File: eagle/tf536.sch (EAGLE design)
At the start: 74 parts, among them IC1 MC68030, IC10 74VHC245PW,118, IC2 LM1117-3.3, IC3 SAMACSYS_PARTS_XC95144XL-10TQ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, IC4 74VHC245PW,118, IC5 74VHC245PW,118, IC6 74VHC245PW,118, IC7 MT48LC16M16A2P-6A_G, IC8 MT48LC16M16A2P-6A_G, IC9 74VHC245PW,118, U1 SN74CB3T3245PW, U2 SN74CB3T3245PW, U3 SN74CB3T3245PW, U4 SN74CB3T3245PW, X1 MC68000

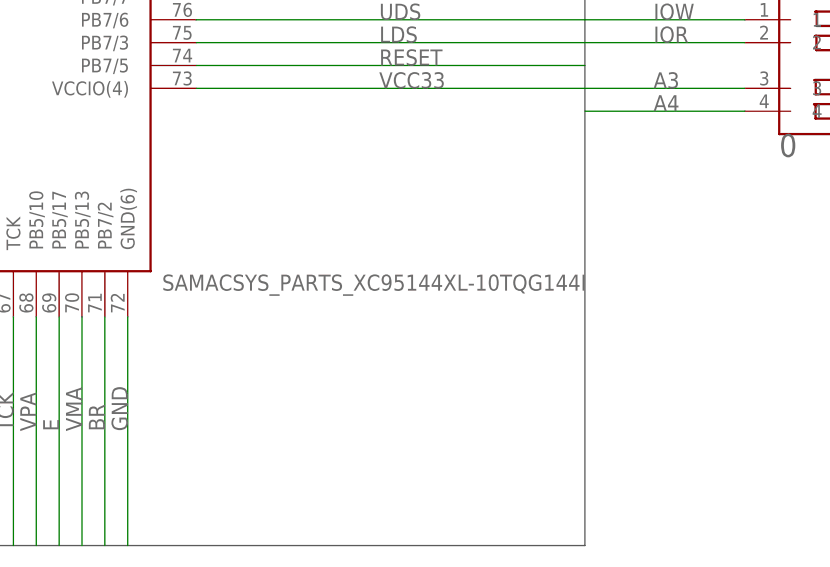
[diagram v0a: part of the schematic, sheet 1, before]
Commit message: Updating the schematic to say XC95288XL
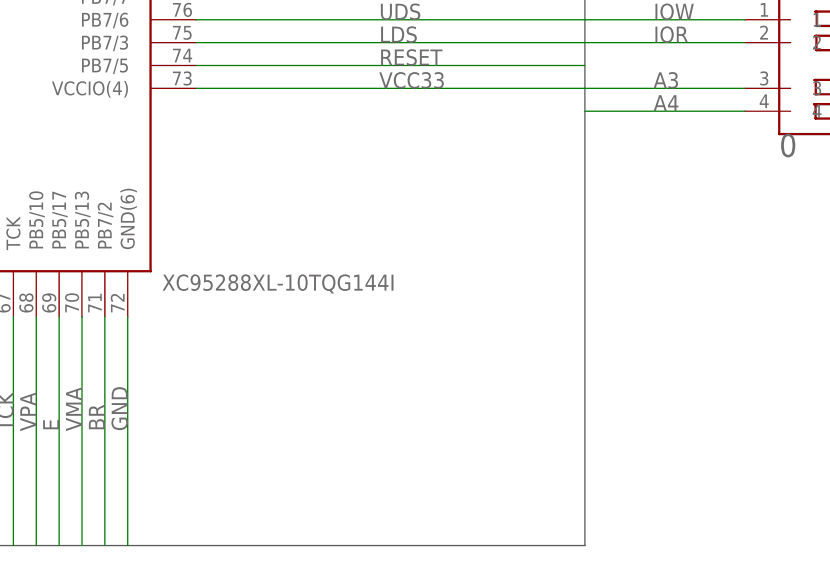
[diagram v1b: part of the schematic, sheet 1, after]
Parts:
- IC3: value SAMACSYS_PARTS_XC95144XL-10TQG144I -> XC95288XL-10TQG144I
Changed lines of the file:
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@@
 <part name="U3" library="SN74CB3T3245PW" deviceset="SN74CB3T3245PW" device=""/>
 <part name="U4" library="SN74CB3T3245PW" deviceset="SN74CB3T3245PW" device=""/>
-<part name="IC3" library="sjl540" deviceset="SAMACSYS_PARTS_XC95144XL-10TQG144I" device=""/>
+<part name="IC3" library="sjl540" deviceset="SAMACSYS_PARTS_XC95144XL-10TQG144I" device="" value="XC95288XL-10TQG144I"/>
 <part name="C8" library="microbuilder" deviceset="CAP_CERAMIC" device="1206" value="1uF"/>
 <part name="C9" library="microbuilder" deviceset="CAP_CERAMIC" device="1206" value="1uF"/>

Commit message: Add Eagle netlist and UCF generation tools
- Add generate_netlist.py to export Eagle schematic to netlist format
- Add generate_ucf.py to generate UCF files from Eagle netlists
  - Filters power (GND, VCC) and JTAG (TCK/TDI/TDO/TMS) signals
  - Handles 68030-specific signals (AS30, BG30, etc.) correctly
  - Optional --remap-dbus flag to map D16-D31 to D<0>-D<15>
- Update Eagle schematic signal names to match UCF conventions:
  - CLK7M -> CLK7M_RAW
  - DS30ACK0/1 -> DSACK0/1
  - Fix DQM0-3 pin mapping
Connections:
- net CLK7M renamed CLK7M_RAW
- net DS30ACK0 renamed DSACK0
- net DS30ACK1 renamed DSACK1
- net DQM0: now also IC3.PB2/6, IC7.DQMH; no longer IC3.PB1/2, IC8.DQML
- net DQM1: now also IC3.PB2/17, IC7.DQML; no longer IC3.PB1/10, IC8.DQMH
- net DQM2: now also IC3.PB1/10, IC8.DQMH; no longer IC3.PB2/17, IC7.DQML
- net DQM3: now also IC3.PB1/2, IC8.DQML; no longer IC3.PB2/6, IC7.DQMH
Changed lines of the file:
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@@
 </instances>
 <busses>
-<bus name="A[0..31],A_BUF[2..4],ACTIVE,AGND,ARAM[0..12],AS,AS20,AS30,AUX[0..1],AVEC,BA[0..1],BERR,BG,BG20,BG30,BGACK,BGACK20,BGACK30,BR,BR20,BR30,BUSEN,CAS,CBACK,CBREQ,CDIS,CFGIN,CFGOUT,CIIN,CIIOUT,CLK7M,CLK14M,CLK50M,CLK100M,CLKCPU,CLKRAM,CLKRAME,D[0..31],DBEN,DIDE[0..15],DQM[0..3],DRAM[0..31],DS20,DS30,DS30ACK[0..1],DSACK[0..1],DTACK,E,FC[0..2],FIRE[0..1],GND,HALT,IDECS,IDECS[0..1],IDECS_BUF[0..1],IDEINT,IDEINT_CLEAN,IDELED,IDEWAIT,INT2,INT6,INTCYCLE,IOR,IOR_BUF,IOW,IOW_BUF,IPL[0..2],LDS,MMUDIS,PUNT,RAMCS,RAMOE,RAMWE,RAS,REFILL,RESET,R/W,RW20,RW30,RXD,RXD_EXT,SIZ[0..1],SPARE,STATUS,STERM,TCK,TDI,TDO,TMS,TXD,TXD_EXT,UDS,VCC,VCC33,VMA,VPA">
+<bus name="A[0..31],A_BUF[2..4],ACTIVE,AGND,ARAM[0..12],AS,AS20,AS30,AUX[0..1],AVEC,BA[0..1],BERR,BG,BG20,BG30,BGACK,BGACK20,BGACK30,BR,BR20,BR30,BUSEN,CAS,CBACK,CBREQ,CDIS,CFGIN,CFGOUT,CIIN,CIIOUT,CLK7M_RAW,CLK14M,CLK50M,CLK100M,CLKCPU,CLKRAM,CLKRAME,D[0..31],DBEN,DIDE[0..15],DQM[0..3],DRAM[0..31],DS20,DS30,DS30ACK[0..1],DSACK[0..1],DTACK,E,FC[0..2],FIRE[0..1],GND,HALT,IDECS,IDECS[0..1],IDECS_BUF[0..1],IDEINT,IDEINT_CLEAN,IDELED,IDEWAIT,INT2,INT6,INTCYCLE,IOR,IOR_BUF,IOW,IOW_BUF,IPL[0..2],LDS,MMUDIS,PUNT,RAMCS,RAMOE,RAMWE,RAS,REFILL,RESET,R/W,RW20,RW30,RXD,RXD_EXT,SIZ[0..1],SPARE,STATUS,STERM,TCK,TDI,TDO,TMS,TXD,TXD_EXT,UDS,VCC,VCC33,VMA,VPA">
 <segment>
 <wire x1="284.48" y1="218.44" x2="469.9" y2="218.44" width="0.762" layer="92"/>
@@
 </segment>
 </net>
-<net name="DS30ACK1" class="0">
+<net name="DSACK1" class="0">
 <segment>
 <pinref part="IC1" gate="G$1" pin="DSACK1"/>
@@
 </segment>
 </net>
-<net name="DS30ACK0" class="0">
+<net name="DSACK0" class="0">
 <segment>
 <pinref part="IC1" gate="G$1" pin="DSACK0"/>
@@
 </segment>
 </net>
-<net name="DQM3" class="0">
+<net name="DQM0" class="0">
 <segment>
 <pinref part="IC3" gate="G$1" pin="PB2/6"/>
@@
 </segment>
 </net>
-<net name="DQM2" class="0">
+<net name="DQM1" class="0">
 <segment>
 <pinref part="IC3" gate="G$1" pin="PB2/17"/>
@@
 </segment>
 </net>
-<net name="DQM0" class="0">
+<net name="DQM3" class="0">
 <segment>
 <pinref part="IC3" gate="G$1" pin="PB1/2"/>
@@
 </segment>
 </net>
-<net name="DQM1" class="0">
+<net name="DQM2" class="0">
 <segment>
 <pinref part="IC3" gate="G$1" pin="PB1/10"/>
@@
 </segment>
 </net>
-<net name="CLK7M" class="0">
+<net name="CLK7M_RAW" class="0">
 <segment>
 <pinref part="IC3" gate="G$1" pin="PB5/7"/>
@@
 </instances>
 <busses>
-<bus name="A[0..31],A_BUF[2..4],ACTIVE,AGND,ARAM[0..12],AS,AS20,AS30,AUX[0..1],AVEC,BA[0..1],BERR,BG,BG20,BG30,BGACK,BGACK20,BGACK30,BR,BR20,BR30,BUSEN,CAS,CBACK,CBREQ,CDIS,CFGIN,CFGOUT,CIIN,CIIOUT,CLK7M,CLK14M,CLK50M,CLK100M,CLKCPU,CLKRAM,CLKRAME,D[0..31],DBEN,DIDE[0..15],DQM[0..3],DRAM[0..31],DS20,DS30,DS30ACK[0..1],DSACK[0..1],DTACK,E,FC[0..2],FIRE[0..1],GND,HALT,IDECS,IDECS[0..1],IDECS_BUF[0..1],IDEINT,IDEINT_CLEAN,IDELED,IDEWAIT,INT2,INT6,INTCYCLE,IOR,IOR_BUF,IOW,IOW_BUF,IPL[0..2],LDS,MMUDIS,PUNT,RAMCS,RAMOE,RAMWE,RAS,REFILL,RESET,R/W,RW20,RW30,RXD,RXD_EXT,SIZ[0..1],SPARE,STATUS,STERM,TCK,TDI,TDO,TMS,TXD,TXD_EXT,UDS,VCC,VCC33,VMA,VPA">
+<bus name="A[0..31],A_BUF[2..4],ACTIVE,AGND,ARAM[0..12],AS,AS20,AS30,AUX[0..1],AVEC,BA[0..1],BERR,BG,BG20,BG30,BGACK,BGACK20,BGACK30,BR,BR20,BR30,BUSEN,CAS,CBACK,CBREQ,CDIS,CFGIN,CFGOUT,CIIN,CIIOUT,CLK7M_RAW,CLK14M,CLK50M,CLK100M,CLKCPU,CLKRAM,CLKRAME,D[0..31],DBEN,DIDE[0..15],DQM[0..3],DRAM[0..31],DS20,DS30,DS30ACK[0..1],DSACK[0..1],DTACK,E,FC[0..2],FIRE[0..1],GND,HALT,IDECS,IDECS[0..1],IDECS_BUF[0..1],IDEINT,IDEINT_CLEAN,IDELED,IDEWAIT,INT2,INT6,INTCYCLE,IOR,IOR_BUF,IOW,IOW_BUF,IPL[0..2],LDS,MMUDIS,PUNT,RAMCS,RAMOE,RAMWE,RAS,REFILL,RESET,R/W,RW20,RW30,RXD,RXD_EXT,SIZ[0..1],SPARE,STATUS,STERM,TCK,TDI,TDO,TMS,TXD,TXD_EXT,UDS,VCC,VCC33,VMA,VPA">
 <segment>
 <wire x1="0" y1="185.42" x2="0" y2="12.7" width="0.762" layer="92"/>
@@
 </segment>
 </net>
-<net name="DQM3" class="0">
+<net name="DQM0" class="0">
 <segment>
 <pinref part="IC7" gate="G$1" pin="DQMH"/>
@@
 </segment>
 </net>
-<net name="DQM2" class="0">
+<net name="DQM1" class="0">
 <segment>
 <pinref part="IC7" gate="G$1" pin="DQML"/>
@@
 </segment>
 </net>
-<net name="DQM1" class="0">
+<net name="DQM2" class="0">
 <segment>
 <pinref part="IC8" gate="G$1" pin="DQMH"/>
@@
 </segment>
 </net>
-<net name="DQM0" class="0">
+<net name="DQM3" class="0">
 <segment>
 <pinref part="IC8" gate="G$1" pin="DQML"/>
@@
 </instances>
 <busses>
-<bus name="A[0..31],AGND,AS,AS20,AVEC,BERR,BG,BG20,BGACK,BR,BURST[2..3],BUSEN,CBACK,CBREQ,CDIS,CIIN,CIIOUT,CLK7M,CLKCPU,CPCS,CPSENSE,D[0..31],D68K[0..15],DBEN,DS20,DSACK[0..1],DTACK,E,FC[0..2],GND,HALT,IDECS[0..1],IDEINT,IDEIOEN,IDELED,IDEWAIT,INT2,INTCYCLE,IOR,IOW,IPL[0..2],LDS,MMUDIS,OVL,RAMCS[0..3],RAMOE,REFILL,RESET,R/W,R/W20,RW30,SIZ[0..1],SPARE,SPI_CLK,SPI_CS[0..1],SPI_MISO,SPI_MOSI,STATUS,STERM,TCK,TDI,TDINT,TDO,TMS,UDS,VCC,VCC18,VCC33,VMA,VPA">
+<bus name="A[0..31],AGND,AS,AS20,AVEC,BERR,BG,BG20,BGACK,BR,BURST[2..3],BUSEN,CBACK,CBREQ,CDIS,CIIN,CIIOUT,CLK7M_RAW,CLKCPU,CPCS,CPSENSE,D[0..31],D68K[0..15],DBEN,DS20,DSACK[0..1],DTACK,E,FC[0..2],GND,HALT,IDECS[0..1],IDEINT,IDEIOEN,IDELED,IDEWAIT,INT2,INTCYCLE,IOR,IOW,IPL[0..2],LDS,MMUDIS,OVL,RAMCS[0..3],RAMOE,REFILL,RESET,R/W,R/W20,RW30,SIZ[0..1],SPARE,SPI_CLK,SPI_CS[0..1],SPI_MISO,SPI_MOSI,STATUS,STERM,TCK,TDI,TDINT,TDO,TMS,UDS,VCC,VCC18,VCC33,VMA,VPA">
 <segment>
 <wire x1="210.82" y1="-5.08" x2="210.82" y2="218.44" width="0.762" layer="92"/>
@@
 </segment>
 </net>
-<net name="CLK7M" class="0">
+<net name="CLK7M_RAW" class="0">
 <segment>
 <pinref part="X1" gate="G$1" pin="CLK"/>
